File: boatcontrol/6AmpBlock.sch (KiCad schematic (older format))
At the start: 13 parts, among them U7901 ULN2803A

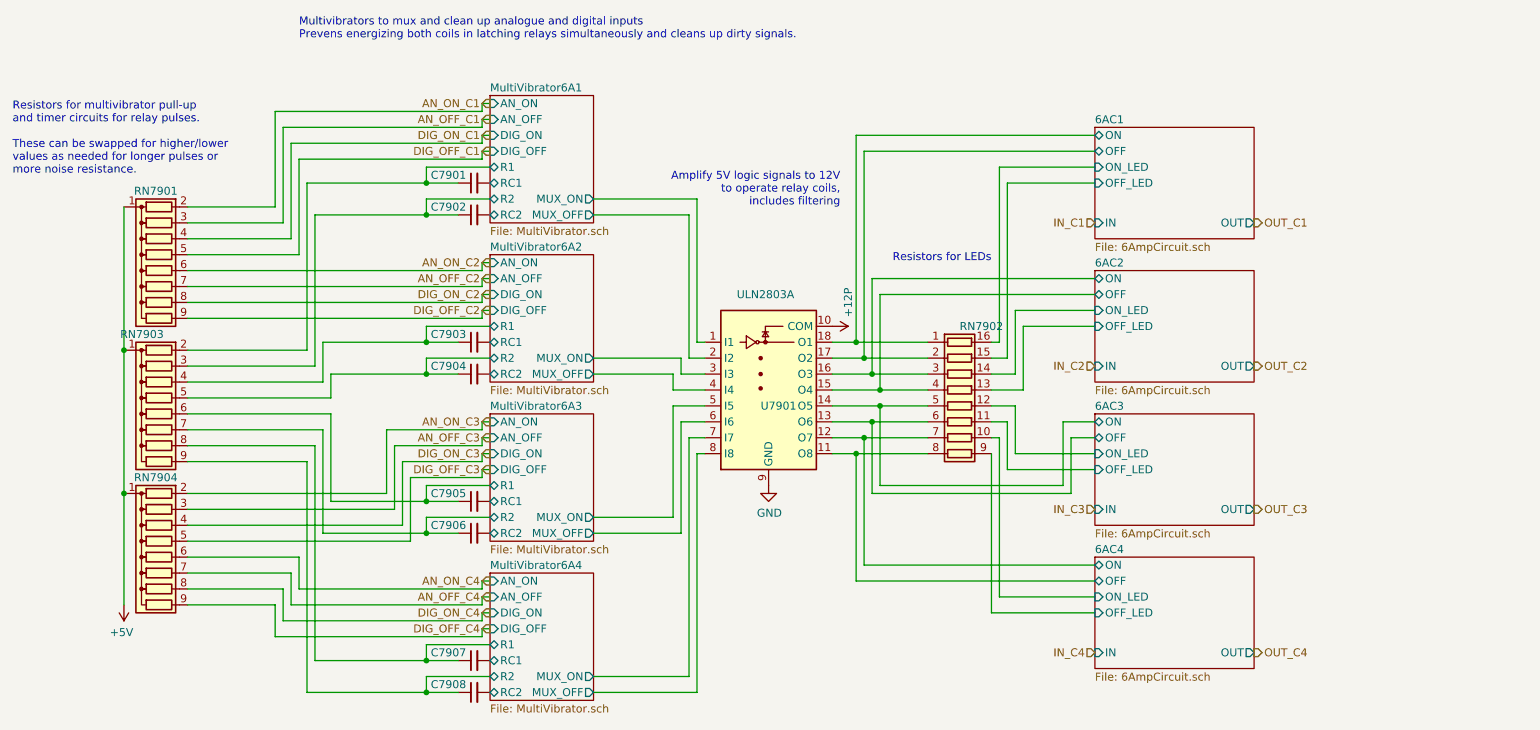
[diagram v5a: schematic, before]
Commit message: Add reverse/AC/DC polarity indicators
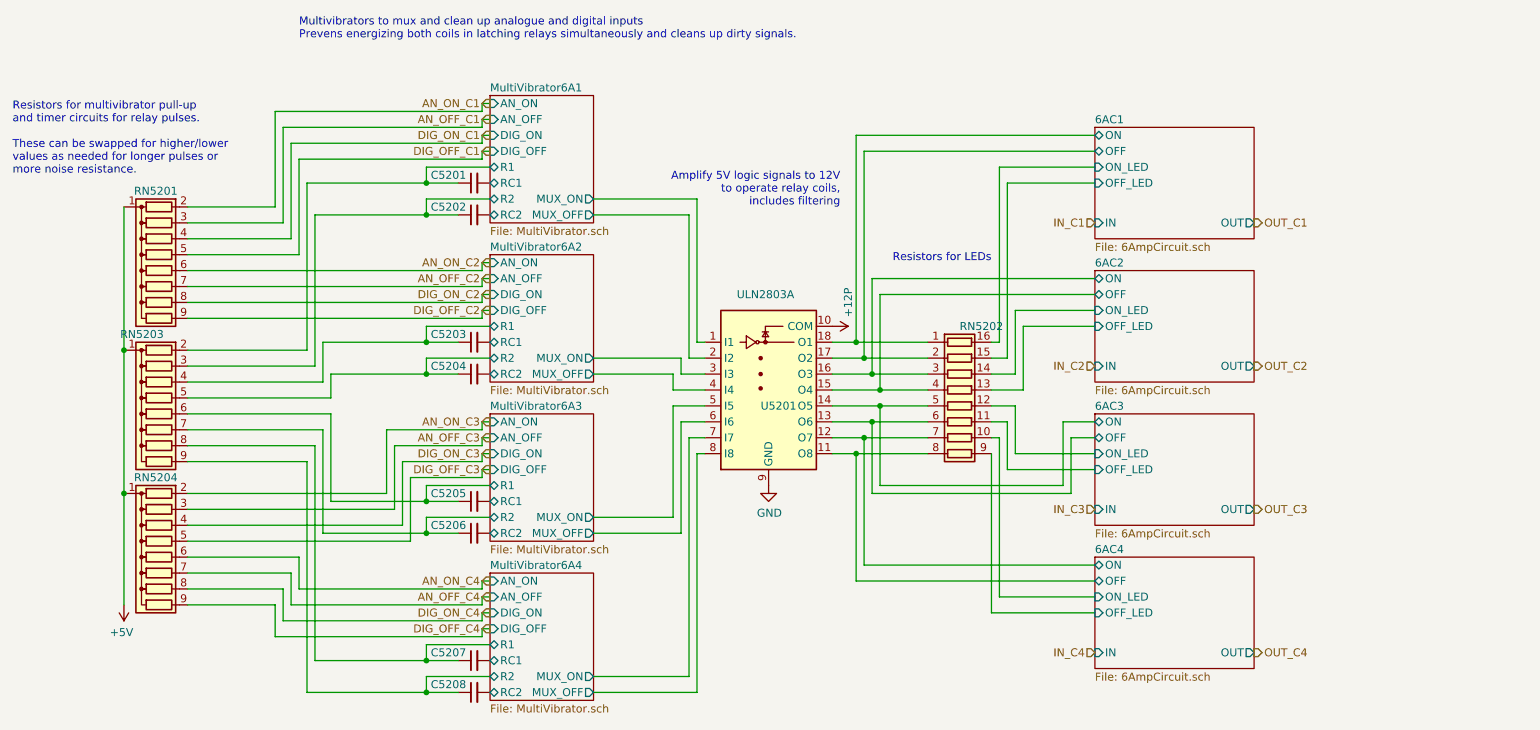
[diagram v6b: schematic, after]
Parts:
- RN7902: value 4116R-1-471 -> 680Ohm; Field4 470 Ohm -> (none); Product (none) -> 4116R-1-681LF‎
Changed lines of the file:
@@
 $Descr A4 11693 8268
 encoding utf-8
-Sheet 79 87
+Sheet 52 87
 Title "Boat Control Hat"
 Date "2020-07-09"
@@
 AR Path="/D1BB8DB4/5F317CB5/60365AE4" Ref="#PWR07901"  Part="1"
 AR Path="/D1BB8DB4/5F746103/60365AE4" Ref="#PWR05201"  Part="1"
-F 0 "#PWR07901" H 6700 3400 50  0001 C CNN
+F 0 "#PWR05201" H 6700 3400 50  0001 C CNN
 F 1 "+12P" H 6550 3650 50  0000 C CNN
 F 2 "" H 6700 3550 50  0001 C CNN
@@
 AR Path="/D1BB8DB4/5F317CB5/60365AF1" Ref="U7901"  Part="1"
 AR Path="/D1BB8DB4/5F746103/60365AF1" Ref="U5201"  Part="1"
-F 0 "U7901" H 6250 3650 50  0000 L CNN
+F 0 "U5201" H 6250 3650 50  0000 L CNN
 F 1 "ULN2803A" H 6100 4350 50  0000 L CNN
 F 2 "Package_DIP:DIP-18_W7.62mm" H 6350 3200 50  0001 L CNN
@@
 AR Path="/D1BB8DB4/5F317CB5/60365B03" Ref="#PWR07902"  Part="1"
 AR Path="/D1BB8DB4/5F746103/60365B03" Ref="#PWR05202"  Part="1"
-F 0 "#PWR07902" H 6300 4300 50  0001 C CNN
+F 0 "#PWR05202" H 6300 4300 50  0001 C CNN
 F 1 "GND" H 6305 4377 50  0000 C CNN
 F 2 "" H 6300 4550 50  0001 C CNN
@@
 AR Path="/D1BB8DB4/5F317CB5/60365B8C" Ref="#PWR07903"  Part="1"
 AR Path="/D1BB8DB4/5F746103/60365B8C" Ref="#PWR05203"  Part="1"
-F 0 "#PWR07903" H 2250 5150 50  0001 C CNN
+F 0 "#PWR05203" H 2250 5150 50  0001 C CNN
 F 1 "+5V" H 2265 5473 50  0000 C CNN
 F 2 "" H 2250 5300 50  0001 C CNN
@@
 AR Path="/D1BB8DB4/5F317CB5/60365C68" Ref="RN7902"  Part="1"
 AR Path="/D1BB8DB4/5F746103/60365C68" Ref="RN5202"  Part="1"
-F 0 "RN7902" V 7000 4050 50  0000 L CNN
-F 1 "4116R-1-471" V 7000 3900 50  0001 L CNN
+F 0 "RN5202" V 7000 4050 50  0000 L CNN
+F 1 "680Ohm" V 7000 3900 50  0001 L CNN
 F 2 "BoatControl:DIP254P762X432-16P" V 7975 4050 50  0001 C CNN
 F 3 "https://www.bourns.com/docs/Product-Datasheets/4100R.pdf" H 7500 4050 50  0001 C CNN
-F 4 "470 Ohm" V 7500 4050 50  0001 C CNN "Field4"
+F 4 "4116R-1-681LF‎" V 7500 4050 50  0001 C CNN "Product"
 	1    7500 4050
 	0    1    1    0
@@
 AR Path="/D1BB8DB4/5F746103/62AB509B" Ref="C5201"  Part="1"
 AR Path="/D1BB8DB4/5F317CB5/62AB509B" Ref="C7901"  Part="1"
-F 0 "C7901" V 4400 2700 50  0000 L CNN
+F 0 "C5201" V 4400 2700 50  0000 L CNN
 F 1 "1uF" H 3600 2550 50  0001 L CNN
 F 2 "Capacitor_THT:C_Disc_D7.5mm_W5.0mm_P5.00mm" H 4450 2650 50  0001 C CNN
@@
 AR Path="/D1BB8DB4/5F746103/62AC1E93" Ref="C5202"  Part="1"
 AR Path="/D1BB8DB4/5F317CB5/62AC1E93" Ref="C7902"  Part="1"
-F 0 "C7902" V 4400 2900 50  0000 L CNN
+F 0 "C5202" V 4400 2900 50  0000 L CNN
 F 1 "1uF" H 3600 2750 50  0001 L CNN
 F 2 "Capacitor_THT:C_Disc_D7.5mm_W5.0mm_P5.00mm" H 4450 2850 50  0001 C CNN
@@
 AR Path="/D1BB8DB4/5F746103/62ADD9A6" Ref="C5208"  Part="1"
 AR Path="/D1BB8DB4/5F317CB5/62ADD9A6" Ref="C7908"  Part="1"
-F 0 "C7908" V 4400 5900 50  0000 L CNN
+F 0 "C5208" V 4400 5900 50  0000 L CNN
 F 1 "1uF" H 3600 5750 50  0001 L CNN
 F 2 "Capacitor_THT:C_Disc_D7.5mm_W5.0mm_P5.00mm" H 4450 5850 50  0001 C CNN
@@
 AR Path="/D1BB8DB4/5F746103/62AEACF8" Ref="C5207"  Part="1"
 AR Path="/D1BB8DB4/5F317CB5/62AEACF8" Ref="C7907"  Part="1"
-F 0 "C7907" V 4400 5700 50  0000 L CNN
+F 0 "C5207" V 4400 5700 50  0000 L CNN
 F 1 "1uF" H 3600 5550 50  0001 L CNN
 F 2 "Capacitor_THT:C_Disc_D7.5mm_W5.0mm_P5.00mm" H 4450 5650 50  0001 C CNN
@@
 AR Path="/D1BB8DB4/5F746103/62AF81A3" Ref="C5206"  Part="1"
 AR Path="/D1BB8DB4/5F317CB5/62AF81A3" Ref="C7906"  Part="1"
-F 0 "C7906" V 4400 4900 50  0000 L CNN
+F 0 "C5206" V 4400 4900 50  0000 L CNN
 F 1 "1uF" H 3600 4750 50  0001 L CNN
 F 2 "Capacitor_THT:C_Disc_D7.5mm_W5.0mm_P5.00mm" H 4450 4850 50  0001 C CNN
@@
 AR Path="/D1BB8DB4/5F746103/62B05762" Ref="C5205"  Part="1"
 AR Path="/D1BB8DB4/5F317CB5/62B05762" Ref="C7905"  Part="1"
-F 0 "C7905" V 4400 4700 50  0000 L CNN
+F 0 "C5205" V 4400 4700 50  0000 L CNN
 F 1 "1uF" H 3600 4550 50  0001 L CNN
 F 2 "Capacitor_THT:C_Disc_D7.5mm_W5.0mm_P5.00mm" H 4450 4650 50  0001 C CNN
@@
 AR Path="/D1BB8DB4/5F746103/62B3C5BA" Ref="C5203"  Part="1"
 AR Path="/D1BB8DB4/5F317CB5/62B3C5BA" Ref="C7903"  Part="1"
-F 0 "C7903" V 4400 3700 50  0000 L CNN
+F 0 "C5203" V 4400 3700 50  0000 L CNN
 F 1 "1uF" H 3600 3550 50  0001 L CNN
 F 2 "Capacitor_THT:C_Disc_D7.5mm_W5.0mm_P5.00mm" H 4450 3650 50  0001 C CNN
@@
 AR Path="/D1BB8DB4/5F746103/62B4996D" Ref="C5204"  Part="1"
 AR Path="/D1BB8DB4/5F317CB5/62B4996D" Ref="C7904"  Part="1"
-F 0 "C7904" V 4400 3900 50  0000 L CNN
+F 0 "C5204" V 4400 3900 50  0000 L CNN
 F 1 "1uF" H 3600 3750 50  0001 L CNN
 F 2 "Capacitor_THT:C_Disc_D7.5mm_W5.0mm_P5.00mm" H 4450 3850 50  0001 C CNN
@@
 AR Path="/D1BB8DB4/5F317CB5/62C7A7CE" Ref="RN7903"  Part="1"
 AR Path="/D1BB8DB4/5F746103/62C7A7CE" Ref="RN5203"  Part="1"
-F 0 "RN7903" V 1950 4050 50  0000 L CNN
+F 0 "RN5203" V 1950 4050 50  0000 L CNN
 F 1 "10M Ohm" H 2100 3700 50  0001 L CNN
 F 2 "Resistor_THT:R_Array_SIP9" V 2925 4100 50  0001 C CNN
@@
 AR Path="/D1BB8DB4/5F317CB5/62F1D24C" Ref="RN7904"  Part="1"
 AR Path="/D1BB8DB4/5F746103/62F1D24C" Ref="RN5204"  Part="1"
-F 0 "RN7904" V 1950 5000 50  0000 C CNN
+F 0 "RN5204" V 1950 5000 50  0000 C CNN
 F 1 "100K Ohm" V 2250 4700 50  0001 C CNN
 F 2 "Resistor_THT:R_Array_SIP9" H 3200 5100 50  0001 L CNN
@@
 AR Path="/D1BB8DB4/5F317CB5/62F2A731" Ref="RN7901"  Part="1"
 AR Path="/D1BB8DB4/5F746103/62F2A731" Ref="RN5201"  Part="1"
-F 0 "RN7901" V 1950 3200 50  0000 C CNN
+F 0 "RN5201" V 1950 3200 50  0000 C CNN
 F 1 "100K Ohm" V 2250 2900 50  0001 C CNN
 F 2 "Resistor_THT:R_Array_SIP9" H 3200 3300 50  0001 L CNN

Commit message: Fix switch layouts
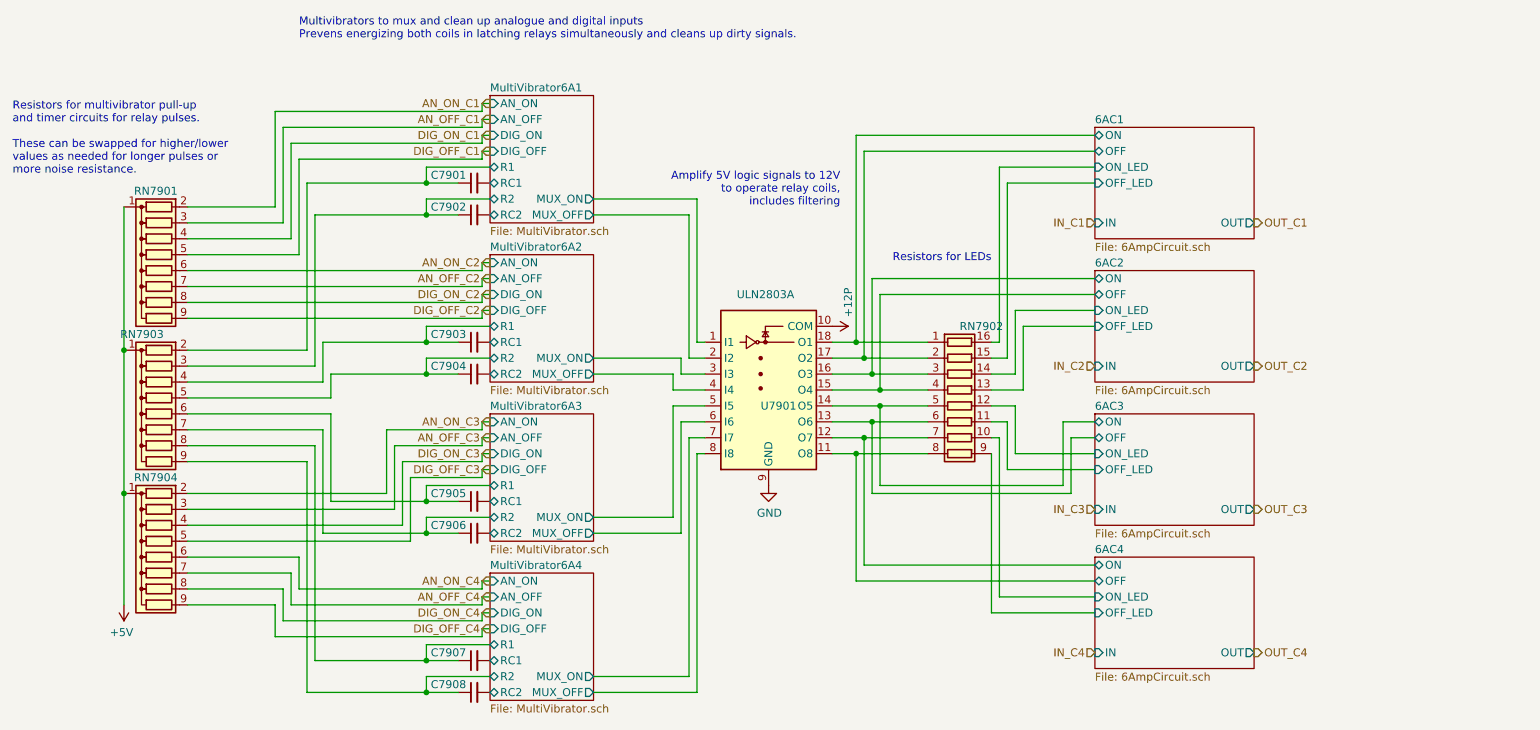
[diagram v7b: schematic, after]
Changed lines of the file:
@@
 $Descr A4 11693 8268
 encoding utf-8
-Sheet 52 87
+Sheet 79 87
 Title "Boat Control Hat"
 Date "2020-07-09"
@@
 AR Path="/D1BB8DB4/5F317CB5/60365AE4" Ref="#PWR07901"  Part="1"
 AR Path="/D1BB8DB4/5F746103/60365AE4" Ref="#PWR05201"  Part="1"
-F 0 "#PWR05201" H 6700 3400 50  0001 C CNN
+F 0 "#PWR07901" H 6700 3400 50  0001 C CNN
 F 1 "+12P" H 6550 3650 50  0000 C CNN
 F 2 "" H 6700 3550 50  0001 C CNN
@@
 AR Path="/D1BB8DB4/5F317CB5/60365AF1" Ref="U7901"  Part="1"
 AR Path="/D1BB8DB4/5F746103/60365AF1" Ref="U5201"  Part="1"
-F 0 "U5201" H 6250 3650 50  0000 L CNN
+F 0 "U7901" H 6250 3650 50  0000 L CNN
 F 1 "ULN2803A" H 6100 4350 50  0000 L CNN
 F 2 "Package_DIP:DIP-18_W7.62mm" H 6350 3200 50  0001 L CNN
@@
 AR Path="/D1BB8DB4/5F317CB5/60365B03" Ref="#PWR07902"  Part="1"
 AR Path="/D1BB8DB4/5F746103/60365B03" Ref="#PWR05202"  Part="1"
-F 0 "#PWR05202" H 6300 4300 50  0001 C CNN
+F 0 "#PWR07902" H 6300 4300 50  0001 C CNN
 F 1 "GND" H 6305 4377 50  0000 C CNN
 F 2 "" H 6300 4550 50  0001 C CNN
@@
 AR Path="/D1BB8DB4/5F317CB5/60365B8C" Ref="#PWR07903"  Part="1"
 AR Path="/D1BB8DB4/5F746103/60365B8C" Ref="#PWR05203"  Part="1"
-F 0 "#PWR05203" H 2250 5150 50  0001 C CNN
+F 0 "#PWR07903" H 2250 5150 50  0001 C CNN
 F 1 "+5V" H 2265 5473 50  0000 C CNN
 F 2 "" H 2250 5300 50  0001 C CNN
@@
 AR Path="/D1BB8DB4/5F317CB5/60365C68" Ref="RN7902"  Part="1"
 AR Path="/D1BB8DB4/5F746103/60365C68" Ref="RN5202"  Part="1"
-F 0 "RN5202" V 7000 4050 50  0000 L CNN
+F 0 "RN7902" V 7000 4050 50  0000 L CNN
 F 1 "680Ohm" V 7000 3900 50  0001 L CNN
 F 2 "BoatControl:DIP254P762X432-16P" V 7975 4050 50  0001 C CNN
@@
 AR Path="/D1BB8DB4/5F746103/62AB509B" Ref="C5201"  Part="1"
 AR Path="/D1BB8DB4/5F317CB5/62AB509B" Ref="C7901"  Part="1"
-F 0 "C5201" V 4400 2700 50  0000 L CNN
+F 0 "C7901" V 4400 2700 50  0000 L CNN
 F 1 "1uF" H 3600 2550 50  0001 L CNN
 F 2 "Capacitor_THT:C_Disc_D7.5mm_W5.0mm_P5.00mm" H 4450 2650 50  0001 C CNN
@@
 AR Path="/D1BB8DB4/5F746103/62AC1E93" Ref="C5202"  Part="1"
 AR Path="/D1BB8DB4/5F317CB5/62AC1E93" Ref="C7902"  Part="1"
-F 0 "C5202" V 4400 2900 50  0000 L CNN
+F 0 "C7902" V 4400 2900 50  0000 L CNN
 F 1 "1uF" H 3600 2750 50  0001 L CNN
 F 2 "Capacitor_THT:C_Disc_D7.5mm_W5.0mm_P5.00mm" H 4450 2850 50  0001 C CNN
@@
 AR Path="/D1BB8DB4/5F746103/62ADD9A6" Ref="C5208"  Part="1"
 AR Path="/D1BB8DB4/5F317CB5/62ADD9A6" Ref="C7908"  Part="1"
-F 0 "C5208" V 4400 5900 50  0000 L CNN
+F 0 "C7908" V 4400 5900 50  0000 L CNN
 F 1 "1uF" H 3600 5750 50  0001 L CNN
 F 2 "Capacitor_THT:C_Disc_D7.5mm_W5.0mm_P5.00mm" H 4450 5850 50  0001 C CNN
@@
 AR Path="/D1BB8DB4/5F746103/62AEACF8" Ref="C5207"  Part="1"
 AR Path="/D1BB8DB4/5F317CB5/62AEACF8" Ref="C7907"  Part="1"
-F 0 "C5207" V 4400 5700 50  0000 L CNN
+F 0 "C7907" V 4400 5700 50  0000 L CNN
 F 1 "1uF" H 3600 5550 50  0001 L CNN
 F 2 "Capacitor_THT:C_Disc_D7.5mm_W5.0mm_P5.00mm" H 4450 5650 50  0001 C CNN
@@
 AR Path="/D1BB8DB4/5F746103/62AF81A3" Ref="C5206"  Part="1"
 AR Path="/D1BB8DB4/5F317CB5/62AF81A3" Ref="C7906"  Part="1"
-F 0 "C5206" V 4400 4900 50  0000 L CNN
+F 0 "C7906" V 4400 4900 50  0000 L CNN
 F 1 "1uF" H 3600 4750 50  0001 L CNN
 F 2 "Capacitor_THT:C_Disc_D7.5mm_W5.0mm_P5.00mm" H 4450 4850 50  0001 C CNN
@@
 AR Path="/D1BB8DB4/5F746103/62B05762" Ref="C5205"  Part="1"
 AR Path="/D1BB8DB4/5F317CB5/62B05762" Ref="C7905"  Part="1"
-F 0 "C5205" V 4400 4700 50  0000 L CNN
+F 0 "C7905" V 4400 4700 50  0000 L CNN
 F 1 "1uF" H 3600 4550 50  0001 L CNN
 F 2 "Capacitor_THT:C_Disc_D7.5mm_W5.0mm_P5.00mm" H 4450 4650 50  0001 C CNN
@@
 AR Path="/D1BB8DB4/5F746103/62B3C5BA" Ref="C5203"  Part="1"
 AR Path="/D1BB8DB4/5F317CB5/62B3C5BA" Ref="C7903"  Part="1"
-F 0 "C5203" V 4400 3700 50  0000 L CNN
+F 0 "C7903" V 4400 3700 50  0000 L CNN
 F 1 "1uF" H 3600 3550 50  0001 L CNN
 F 2 "Capacitor_THT:C_Disc_D7.5mm_W5.0mm_P5.00mm" H 4450 3650 50  0001 C CNN
@@
 AR Path="/D1BB8DB4/5F746103/62B4996D" Ref="C5204"  Part="1"
 AR Path="/D1BB8DB4/5F317CB5/62B4996D" Ref="C7904"  Part="1"
-F 0 "C5204" V 4400 3900 50  0000 L CNN
+F 0 "C7904" V 4400 3900 50  0000 L CNN
 F 1 "1uF" H 3600 3750 50  0001 L CNN
 F 2 "Capacitor_THT:C_Disc_D7.5mm_W5.0mm_P5.00mm" H 4450 3850 50  0001 C CNN
@@
 AR Path="/D1BB8DB4/5F317CB5/62C7A7CE" Ref="RN7903"  Part="1"
 AR Path="/D1BB8DB4/5F746103/62C7A7CE" Ref="RN5203"  Part="1"
-F 0 "RN5203" V 1950 4050 50  0000 L CNN
+F 0 "RN7903" V 1950 4050 50  0000 L CNN
 F 1 "10M Ohm" H 2100 3700 50  0001 L CNN
 F 2 "Resistor_THT:R_Array_SIP9" V 2925 4100 50  0001 C CNN
@@
 AR Path="/D1BB8DB4/5F317CB5/62F1D24C" Ref="RN7904"  Part="1"
 AR Path="/D1BB8DB4/5F746103/62F1D24C" Ref="RN5204"  Part="1"
-F 0 "RN5204" V 1950 5000 50  0000 C CNN
+F 0 "RN7904" V 1950 5000 50  0000 C CNN
 F 1 "100K Ohm" V 2250 4700 50  0001 C CNN
 F 2 "Resistor_THT:R_Array_SIP9" H 3200 5100 50  0001 L CNN
@@
 AR Path="/D1BB8DB4/5F317CB5/62F2A731" Ref="RN7901"  Part="1"
 AR Path="/D1BB8DB4/5F746103/62F2A731" Ref="RN5201"  Part="1"
-F 0 "RN5201" V 1950 3200 50  0000 C CNN
+F 0 "RN7901" V 1950 3200 50  0000 C CNN
 F 1 "100K Ohm" V 2250 2900 50  0001 C CNN
 F 2 "Resistor_THT:R_Array_SIP9" H 3200 3300 50  0001 L CNN

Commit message: Fix LED resistors
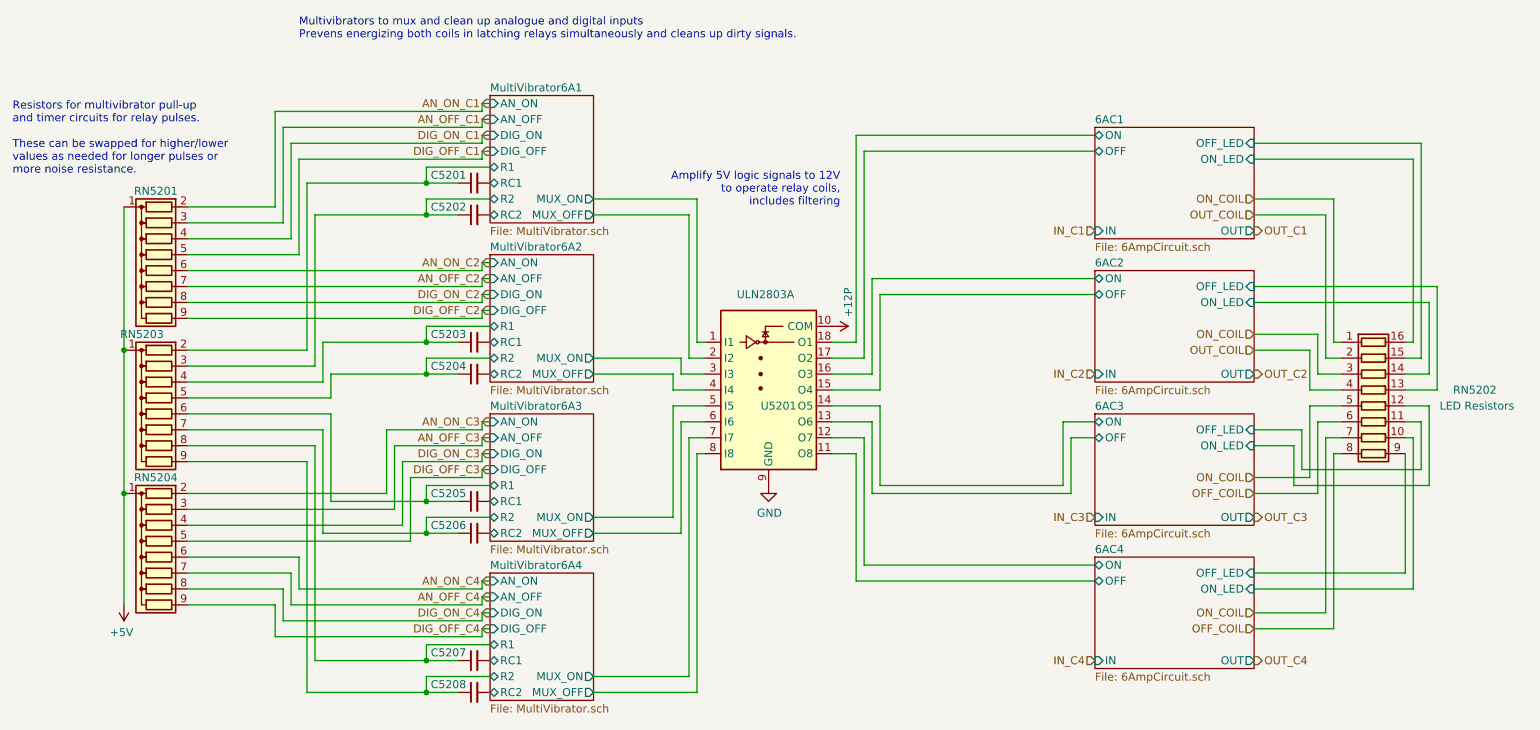
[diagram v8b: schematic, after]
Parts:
- RN7902: Purpose (none) -> LED Resistors
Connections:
- net 6AC1/OFF: no longer RN7902.2 (R2.1)
- net 6AC1/ON: no longer RN7902.1 (R1.1)
- net 6AC2/OFF: no longer RN7902.4 (R4.1)
- net 6AC2/ON: no longer RN7902.3 (R3.1)
- net 6AC3/OFF: no longer RN7902.6 (R6.1)
- net 6AC3/ON: no longer RN7902.5 (R5.1)
- net 6AC4/OFF: no longer RN7902.8 (R8.1)
- net 6AC4/ON: no longer RN7902.7 (R7.1)
- new net OFF_COIL: RN7902.6 (R6.1), RN7902.8 (R8.1)
- new net ON_COIL: RN7902.1 (R1.1), RN7902.3 (R3.1), RN7902.5 (R5.1), RN7902.7 (R7.1)
- new net OUT_COIL: RN7902.2 (R2.1), RN7902.4 (R4.1)
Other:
- note removed: "Resistors for LEDs"
- moved on the sheet: RN5202
